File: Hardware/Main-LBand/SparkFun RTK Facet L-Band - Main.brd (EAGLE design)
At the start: 59.5 x 43 mm, 143 parts, among them J1 QWIIC_RIGHT_ANGLE, J2 U.FL, J9 CORTEX_JTAG_DEBUG_PTH, Q2 MBT3904DW1T1, Q3 SIL2308, U1 74HC4052D, U10 MCP73833, U12 SPX3819M5_3_3, U13 POWER-DIVIDER, U2 SPX3819M5_3_3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

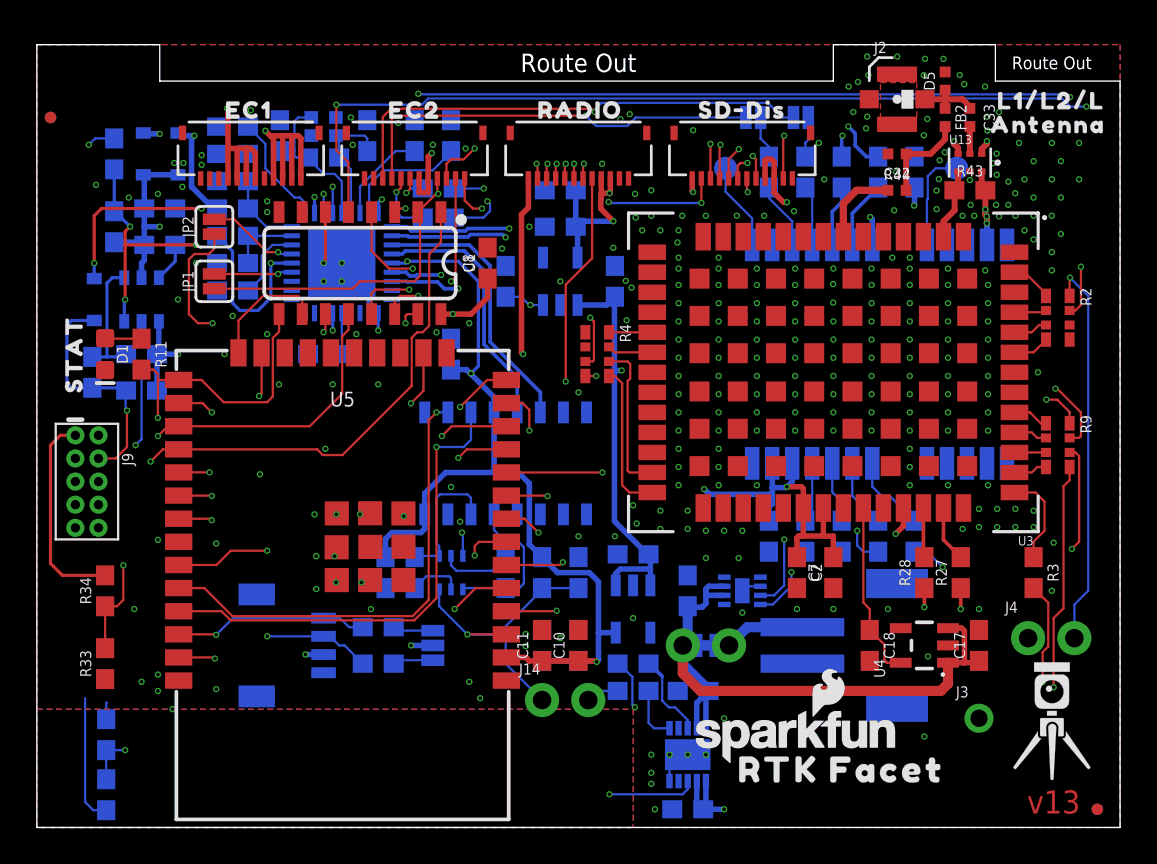
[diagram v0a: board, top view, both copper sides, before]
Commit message: Remove R1, change charger FP, change 33 discretes, ESP32 DFM paste.
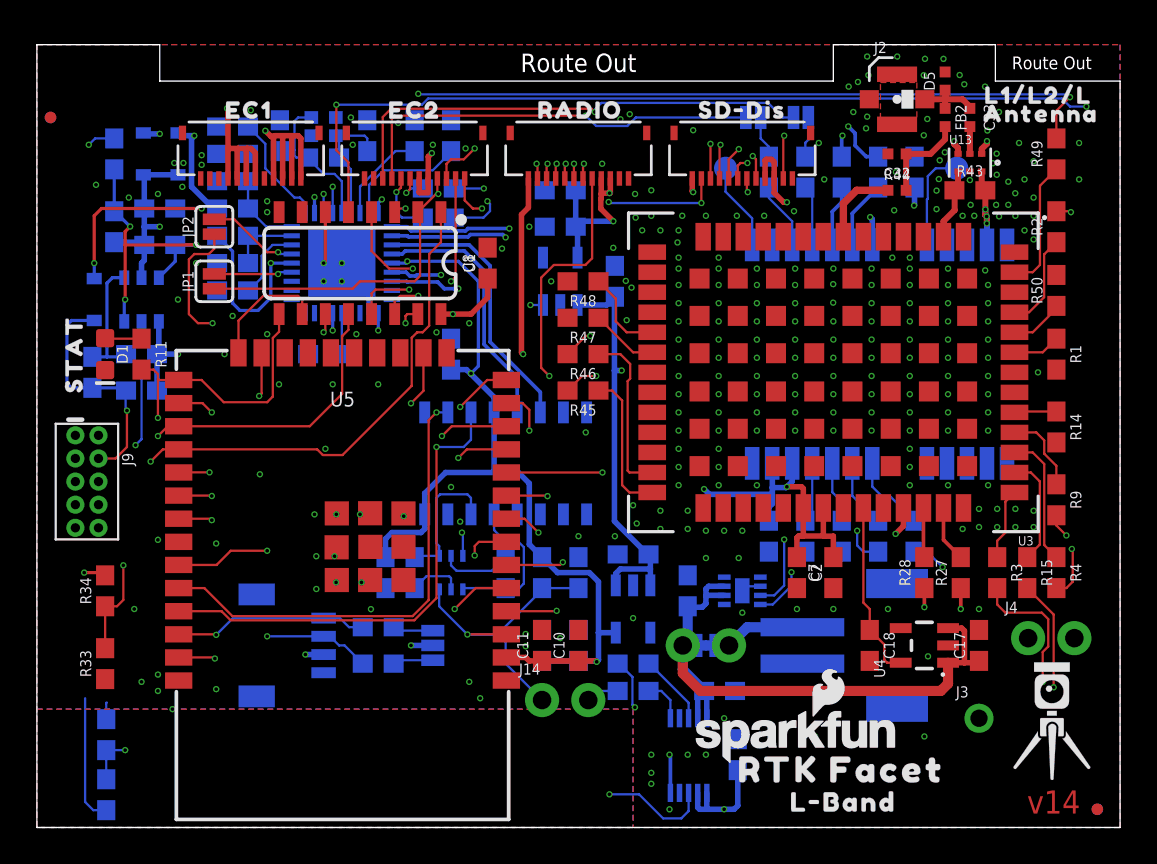
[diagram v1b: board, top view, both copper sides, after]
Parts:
- added R14, R15, R45, R46, R47, R48, R49, R50: 33, SparkFun-Resistors:0603
- added U$5, U$7: (no value), output:L#BAND0
- R1: value DNP -> 33
- R2, R4, R9: device SparkFun-Resistors:1206_RA -> SparkFun-Resistors:0603
- R33: value 20k -> 33k
- U10: value MCP73833 -> MCP73833MSOP; device SparkFun-IC-Power:DFN-10 -> SparkFun-IC-Power:MSOP10
- U12, U2: value SPX3819M5_3_3 -> AP2112K-3.3V
- U4: value SPX3819M5_3_3 -> STLQ015-3.3V
- U5: value ESP-WROOM-3232D -> ESP-WROOM-3232D-DFMP; device SparkFun-RF:ESP-WROOM-32D -> SparkFun-RF:ESP-WROOM-32D-DFM_PASTE
- U9: device SparkFun-GPS:NEO-M9N/M8T/M8U/D9S -> SparkFun-GPS:NEO-M9N/M8T/M8U/D9S/F9P
- moved R1 30.5 mm to (56.0, 26.0), flipped to the top
- moved R4 28.0 mm to (56.0, 14.0)
- moved R2 5.00 mm to (56.0, 33.0), turned to 90 degrees
- moved C16 4.07 mm to (38.5, 4.00), turned to 90 degrees
- moved R9 3.00 mm to (56.0, 18.0)
- moved R3 2.00 mm to (52.8, 14.0)
- moved C3 1.45 mm to (37.5, 7.50), turned to 180 degrees
- moved U$18 0.76 mm to (55.0, 40.2)
- moved U$17 0.72 mm to (55.2, 39.2)
- moved U10 0.07 mm to (35.8, 3.95), turned to 0 degrees
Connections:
- net ESP_14/PERIPHERAL_POWER/MTMS: no longer R1.2
- net ESP_17/ZED_RXI1: now also R15.2; no longer R9.P5
- net ESP_21/SDA: now also R4.2; no longer R9.P6
- net ESP_22/SCL: now also R9.2; no longer R9.P7
- net FENCE_LV: now also R48.1; no longer R4.P8
- net GND: no longer R1.1, U10.11
- net N$16: now also R1.1; no longer R2.P4
- net N$18: now also R50.1; no longer R2.P3
- net N$22: now also R14.1; no longer R9.P1
- net N$5: now also R2.1; no longer R2.P2
- net PPS: now also R49.1; no longer R2.P1
- net RTK_LV: now also R47.1; no longer R4.P7
- net RX2_LV: now also R46.1; no longer R4.P6
- net RXLV: now also R15.1; no longer R9.P4
- net SCL_LV: now also R9.1; no longer R9.P2
- net SDA_LV: now also R4.1; no longer R9.P3
- net TX2_LV: now also R45.1; no longer R4.P5
- net ZED_!RESET!: now also R1.2; no longer R2.P5
- net ZED_!SAFE!: now also R50.2; no longer R2.P6
- net ZED_EXTINT: now also R2.2; no longer R2.P7
- net ZED_FENCE_STAT: now also R48.2; no longer R4.P1
- net ZED_PPS_STAT: now also R49.2; no longer R2.P8
- net ZED_RTK_STAT: now also R47.2; no longer R4.P2
- net ZED_RXI2: now also R46.2; no longer R4.P3
- net ZED_TXO2: now also R45.2; no longer R4.P4
- net ZED_TX_READY: now also R14.2; no longer R9.P8
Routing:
- net ZED_TX_READY: track 12.8 -> 0.00 mm, vias 2 -> 0
- net ESP_22/SCL: track 143.9 -> 133.7 mm, vias 11 -> 10
- net ESP_17/ZED_RXI1: track 102.2 -> 95.7 mm
- net SDA_LV: track 1.73 -> 7.29 mm
- net PPS: track 2.34 -> 7.19 mm
- net ZED_EXTINT: track 59.5 -> 54.7 mm
- net RXLV: track 1.85 -> 6.04 mm
- net N$5: track 1.77 -> 5.27 mm
- net ESP_21/SDA: track 143.2 -> 140.2 mm
- net ZED_PPS_STAT: track 80.6 -> 83.6 mm, vias 4 -> 3
- net SCL_LV: track 1.85 -> 4.51 mm
- net FENCE_LV: track 2.37 -> 4.84 mm
- net ESP_16/ZED_TXO1: track 83.9 -> 85.9 mm
- net ESP_14/PERIPHERAL_POWER/MTMS: track 35.5 -> 34.0 mm
- net V_RAW: track 77.2 -> 78.7 mm
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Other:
- board text added: "Finish: ENIG"
- board text added: "Material: TG155"
- board text added: "Soldermask: Red"
- board text added: "Stackup: JLC7628 Impedence Controlled"
- board text added: "v14"
- board text removed: "ENIG Finish"
- board text removed: "Impedance controlled: JLC7628"
- board text removed: "v13"

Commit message: Close jumpers between ZED/NEO. Change resistor IDs to indicate L-Band Direct.
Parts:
- JP3, JP4: device SparkFun-Jumpers:SMT-JUMPER_2_NO_SILK -> SparkFun-Jumpers:SMT-JUMPER_2_NC_TRACE_SILK
- R33: value 33k -> 100k
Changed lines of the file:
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@@
 <attribute name="VALUE" x="0.0362" y="20.8288" size="0.6096" layer="27" font="vector" ratio="20" rot="R270"/>
 </element>
-<element name="R33" library="SparkFun-Resistors" package="0603" value="33k" x="3.75" y="9" smashed="yes" rot="R90">
+<element name="R33" library="SparkFun-Resistors" package="0603" value="100k" x="3.75" y="9" smashed="yes" rot="R90">
 <attribute name="NAME" x="2.988" y="9" size="0.6096" layer="25" font="vector" ratio="20" rot="R90" align="bottom-center"/>
-<attribute name="PROD_ID" value="RES-08416" x="3.75" y="9" size="1.778" layer="27" font="vector" ratio="15" rot="R90" display="off"/>
-<attribute name="VALUE" value="33k" x="4.512" y="9" size="0.6096" layer="27" font="vector" ratio="20" rot="R90" align="top-center"/>
+<attribute name="PROD_ID" value="RES-07828" x="3.75" y="9" size="1.778" layer="27" font="vector" ratio="15" rot="R90" display="off"/>
+<attribute name="VALUE" value="100k" x="4.512" y="9" size="0.6096" layer="27" font="vector" ratio="20" rot="R90" align="top-center"/>
 </element>
 <element name="R34" library="SparkFun-Resistors" package="0603" value="10k" x="3.75" y="13" smashed="yes" rot="R90">
@@
 <element name="U$17" library="output" package="ANTENNA1" value="" x="55.151" y="39.208" smashed="yes"/>
 <element name="U$18" library="output" package="L1#L2#L0" value="" x="55.01" y="40.22" smashed="yes"/>
-<element name="JP3" library="SparkFun-Jumpers" package="SMT-JUMPER_2_NO_SILK" package3d_urn="urn:adsk.eagle:package:39279/1" value="" x="39.35" y="39" smashed="yes" rot="MR0">
+<element name="JP3" library="SparkFun-Jumpers" package="SMT-JUMPER_2_NC_TRACE_SILK" package3d_urn="urn:adsk.eagle:package:39281/1" value="" x="39.35" y="39" smashed="yes" rot="MR0">
 <attribute name="NAME" x="39.35" y="40.143" size="0.6096" layer="26" font="vector" ratio="20" rot="MR0" align="bottom-center"/>
 <attribute name="VALUE" x="39.35" y="37.857" size="0.6096" layer="28" font="vector" ratio="20" rot="MR0" align="top-center"/>
 </element>
-<element name="JP4" library="SparkFun-Jumpers" package="SMT-JUMPER_2_NO_SILK" package3d_urn="urn:adsk.eagle:package:39279/1" value="" x="41.97" y="39" smashed="yes" rot="MR0">
+<element name="JP4" library="SparkFun-Jumpers" package="SMT-JUMPER_2_NC_TRACE_SILK" package3d_urn="urn:adsk.eagle:package:39281/1" value="" x="41.97" y="39" smashed="yes" rot="MR0">
 <attribute name="NAME" x="41.97" y="40.143" size="0.6096" layer="26" font="vector" ratio="20" rot="MR0" align="bottom-center"/>
 <attribute name="VALUE" x="41.97" y="37.857" size="0.6096" layer="28" font="vector" ratio="20" rot="MR0" align="top-center"/>
@@
 <via x="30.65" y="39.3" extent="1-16" drill="0.2"/>
 <contactref element="JP4" pad="2"/>
-<wire x1="41.5636" y1="39" x2="40.9636" y2="39" width="0.127" layer="16"/>
+<wire x1="41.4493" y1="39" x2="40.9636" y2="39" width="0.127" layer="16"/>
 <wire x1="40.1635" y1="39.8001" x2="40.9636" y2="39" width="0.127" layer="16"/>
 <wire x1="40.1635" y1="39.8001" x2="31.01190625" y2="39.8001" width="0.127" layer="16"/>
@@
 <wire x1="30.15" y1="39.1" x2="30.2214" y2="39.1" width="0.127" layer="15"/>
 <contactref element="JP3" pad="2"/>
-<wire x1="38.9436" y1="39" x2="32.89999375" y2="39" width="0.127" layer="16"/>
+<wire x1="38.8293" y1="39" x2="32.89999375" y2="39" width="0.127" layer="16"/>
 <wire x1="32.89999375" y1="39" x2="32.43329375" y2="38.5333" width="0.127" layer="16"/>
 <wire x1="32.43329375" y1="38.5333" x2="30.7167" y2="38.5333" width="0.127" layer="16"/>
@@
 <contactref element="R41" pad="2"/>
 <contactref element="JP3" pad="1"/>
-<wire x1="40.21" y1="36.85" x2="40.21" y2="37.39" width="0.127" layer="16"/>
-<wire x1="39.7564" y1="37.8436" x2="39.7564" y2="39" width="0.127" layer="16"/>
-<wire x1="40.21" y1="37.39" x2="39.7564" y2="37.8436" width="0.127" layer="16"/>
+<wire x1="40.21" y1="37.39" x2="40.21" y2="36.85" width="0.127" layer="16"/>
+<wire x1="39.8707" y1="39" x2="39.8707" y2="37.7293" width="0.127" layer="16"/>
+<wire x1="39.8707" y1="37.7293" x2="40.21" y2="37.39" width="0.127" layer="16"/>
 </signal>
 <signal name="N$35">
 <contactref element="R42" pad="2"/>
 <contactref element="JP4" pad="1"/>
-<wire x1="42.21" y1="36.85" x2="42.21" y2="37.61" width="0.127" layer="16"/>
-<wire x1="42.21" y1="37.61" x2="42.4" y2="37.8" width="0.127" layer="16"/>
-<wire x1="42.4" y1="37.8" x2="42.4" y2="38.9764" width="0.127" layer="16"/>
-<wire x1="42.4" y1="38.9764" x2="42.3764" y2="39" width="0.127" layer="16"/>
+<wire x1="42.21" y1="37.61" x2="42.21" y2="36.85" width="0.127" layer="16"/>
+<wire x1="42.4907" y1="39" x2="42.4907" y2="37.8907" width="0.127" layer="16"/>
+<wire x1="42.4907" y1="37.8907" x2="42.21" y2="37.61" width="0.127" layer="16"/>
 </signal>
 <signal name="ZED_!RESET!">
